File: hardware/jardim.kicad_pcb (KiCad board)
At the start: 2 copper layers, 100 x 100 mm, 81 parts, among them J1 DC_INPUT, J10 DHT22_AMB, J11 LIGHT_SENSOR_1, J12 LIGHT_SENSOR_2, J13 LEVEL_SENSOR_1, J14 LEVEL_SENSOR_2, J15 SOIL_HUMIDITY_SENSOR_1, J16 SOIL_HUMIDITY_SENSOR_2, J2 PUMP_1, J3 PUMP_2, J4 LIGHT_1, J5 LIGHT_2, J6 HEAT_1, J7 HEAT_2, J8 DS12B20_2, J9 DS18B20_1, Q1 FQP30N06L, Q2 FQP30N06L, Q3 FQP30N06L, Q4 FQP30N06L, Q5 FQP30N06L, Q6 FQP30N06L, Q7 FQP30N06L, SW1 SW_Push, SW2 SW_Push, SW3 SW_Push, SW4 SW_SPST, U1 AM2302, U2 DM-OLED096-636

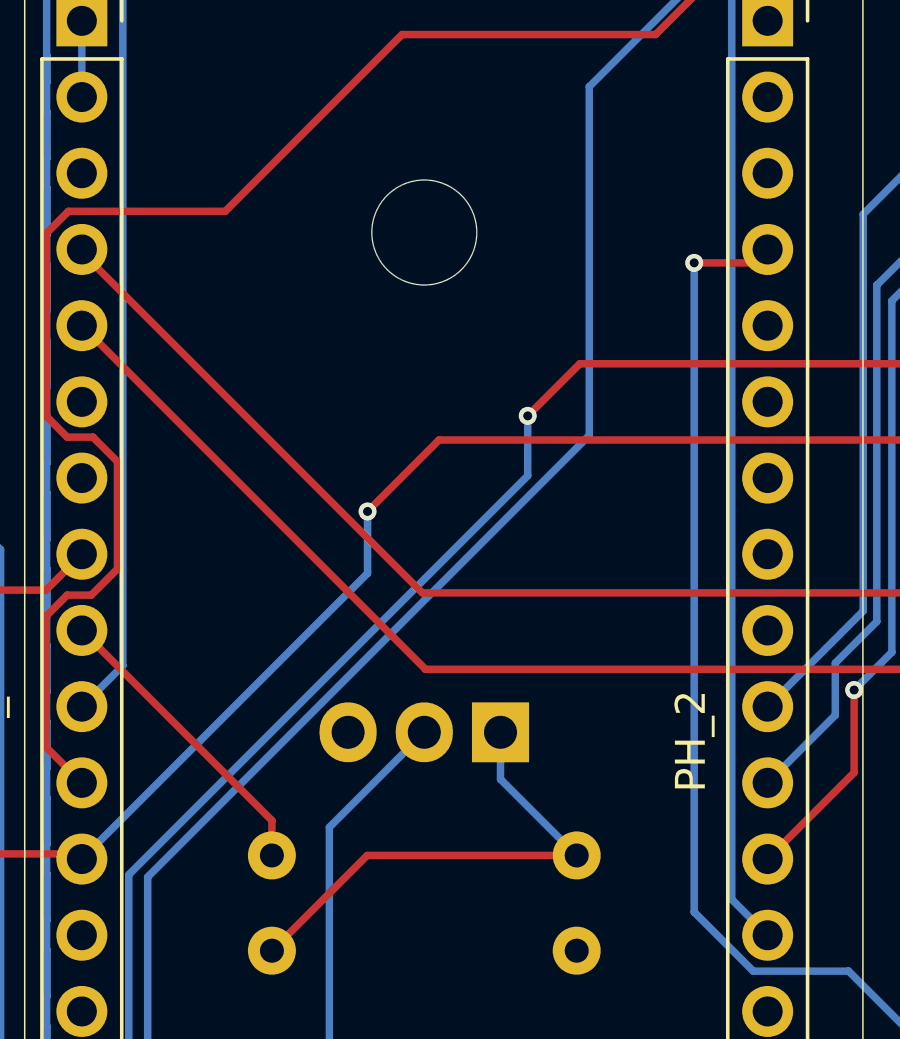
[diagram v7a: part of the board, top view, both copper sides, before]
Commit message: refazendo os conectores de perifericos. atualmente luz 1 concluida
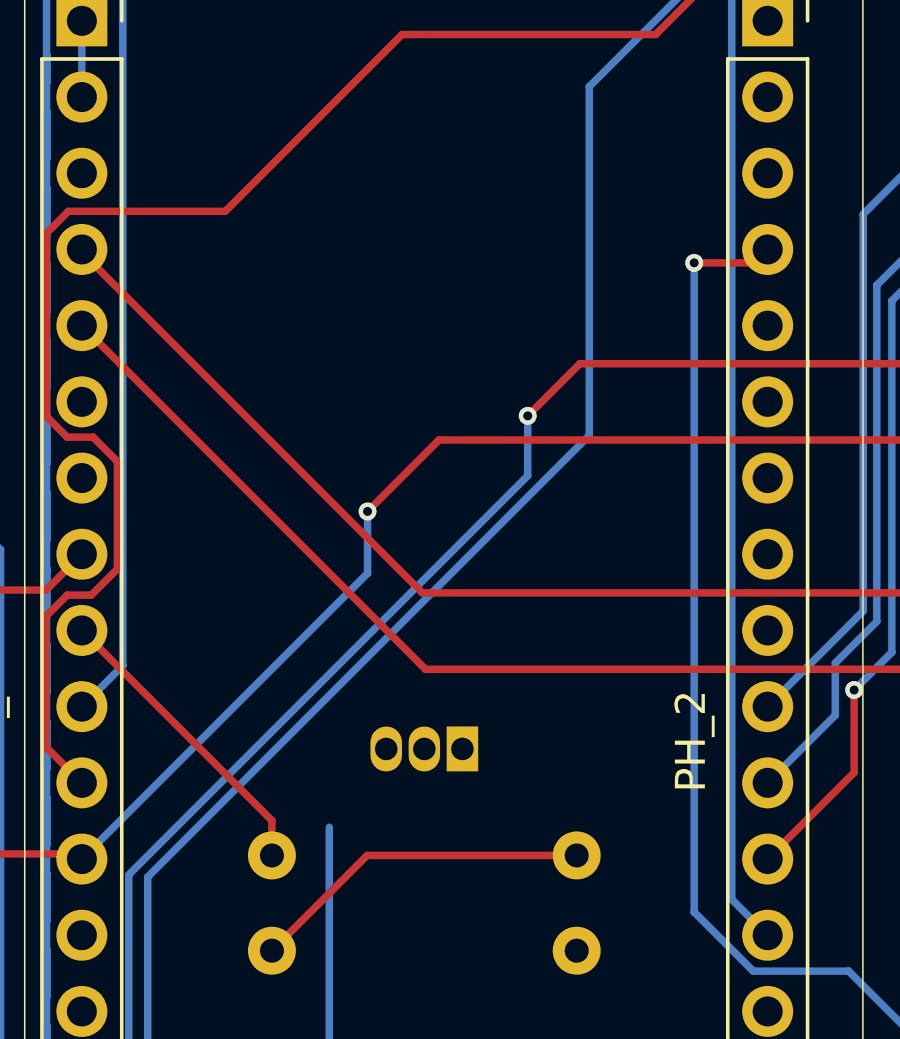
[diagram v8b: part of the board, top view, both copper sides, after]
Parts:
- Q7: value FQP30N06L -> BC337; footprint Package_TO_SOT_THT:TO-220-3_Horizontal_TabDown -> Package_TO_SOT_THT:TO-92_Inline_Horizontal2
- moved Q7 1.39 mm to (159.4, 105.7)
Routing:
- net Net-(Q7-G): track 16.6 -> 11.5 mm
- net Net-(BZ1--): track 28.9 -> 24.4 mm
